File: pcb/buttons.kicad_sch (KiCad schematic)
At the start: 15 parts, among them SW2 PLAY, SW4 STOP, SW5 NEXT, SW6 PREV, SW7 VOLDEC, SW8 VOLINC, SW9 POWER

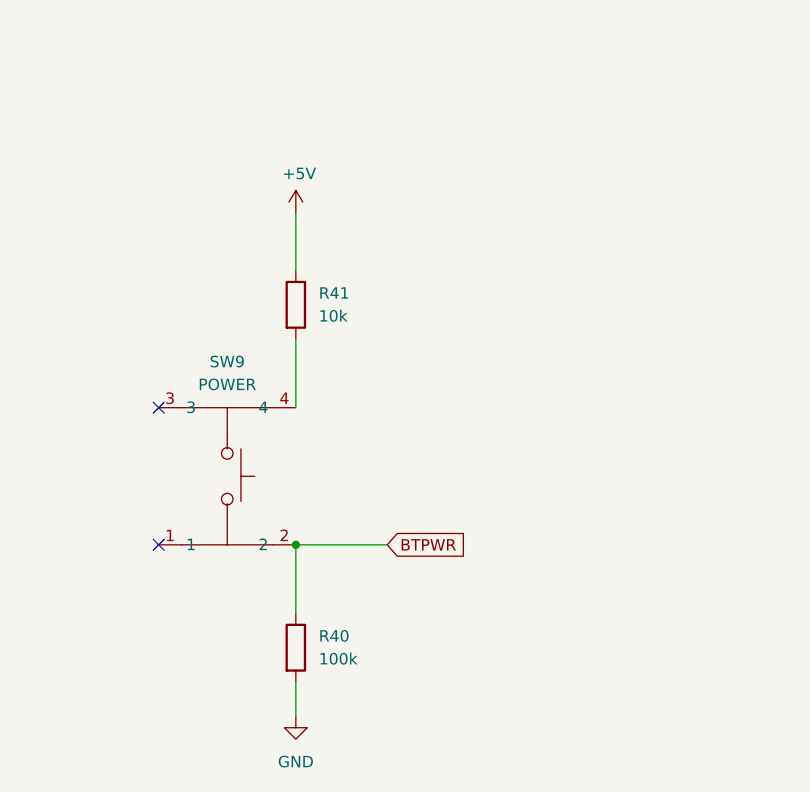
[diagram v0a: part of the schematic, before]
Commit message: Added last minor patches like ideal diode on PCB, added backplate
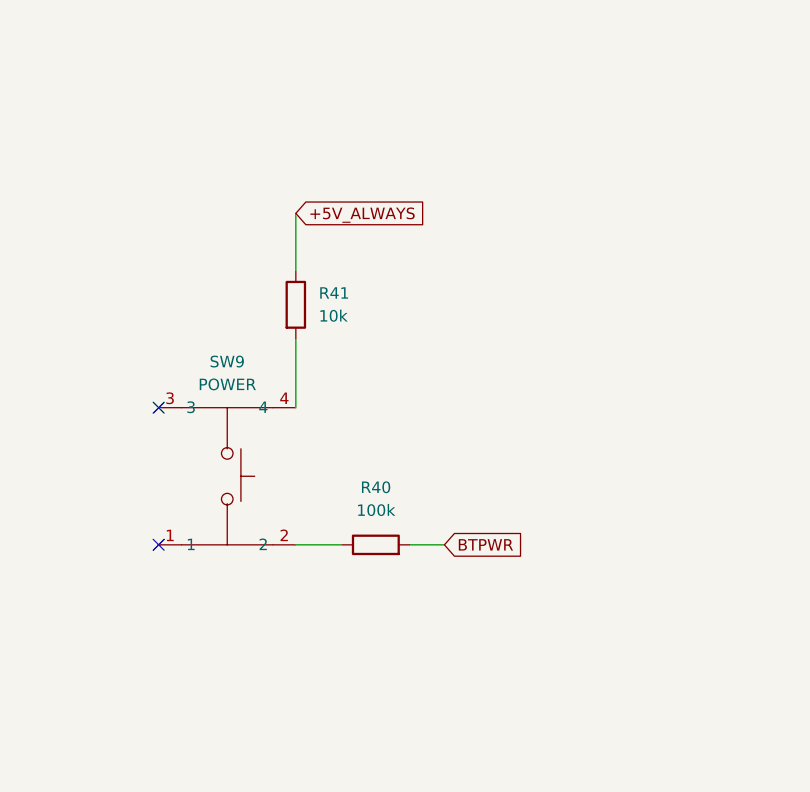
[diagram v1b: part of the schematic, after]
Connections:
- net BTPWR: now also R40.2; no longer R40.1, SW9.2
- net GND: no longer R40.2
- net +5V renamed +5V_ALWAYS
- new net: R40.1, SW9.2
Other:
- moved on the sheet: R40
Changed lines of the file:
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@@
-		(color 0 0 0 0)
-	)
-	(junction
-		(at 78.74 152.4)
-		(diameter 0)
 		(color 0 0 0 0)
 	)
@@
 	(wire
 		(pts
-			(xy 88.9 152.4) (xy 78.74 152.4)
-		)
-		(stroke
-			(width 0)
-			(type default)
-		)
-	)
-	(wire
-		(pts
 			(xy 119.38 49.53) (xy 119.38 57.15)
 		)
@@
 	(wire
 		(pts
-			(xy 78.74 152.4) (xy 78.74 160.02)
+			(xy 91.44 152.4) (xy 95.25 152.4)
 		)
 		(stroke
@@
 	(wire
 		(pts
-			(xy 78.74 167.64) (xy 78.74 171.45)
-		)
-		(stroke
-			(width 0)
-			(type default)
-		)
-	)
-	(wire
-		(pts
 			(xy 156.21 49.53) (xy 168.91 49.53)
 		)
@@
 	(wire
 		(pts
+			(xy 78.74 152.4) (xy 83.82 152.4)
+		)
+		(stroke
+			(width 0)
+			(type default)
+		)
+	)
+	(wire
+		(pts
 			(xy 119.38 49.53) (xy 132.08 49.53)
 		)
@@
 			(width 0)
 			(type default)
+		)
+	)
+	(global_label "+5V_ALWAYS"
+		(shape input)
+		(at 78.74 115.57 0)
+		(fields_autoplaced yes)
+		(effects
+			(font
+				(size 1.27 1.27)
+			)
+			(justify left)
+		)
+		(property "Intersheetrefs" "${INTERSHEET_REFS}"
+			(at 93.5181 115.57 0)
+			(effects
+				(font
+					(size 1.27 1.27)
+				)
+				(justify left)
+				(hide yes)
+			)
 		)
 	)
@@
 	(global_label "BTPWR"
 		(shape input)
-		(at 88.9 152.4 0)
+		(at 95.25 152.4 0)
 		(fields_autoplaced yes)
 		(effects
@@
 		)
 		(property "Intersheetrefs" "${INTERSHEET_REFS}"
-			(at 98.1142 152.4 0)
+			(at 104.4642 152.4 0)
 			(effects
 				(font
@@
 	)
 	(symbol
-		(lib_id "power:+5V")
-		(at 78.74 115.57 0)
-		(unit 1)
-		(exclude_from_sim no)
-		(in_bom yes)
-		(on_board yes)
-		(dnp no)
-		(property "Reference" "#PWR092"
-			(at 78.74 119.38 0)
-			(effects
-				(font
-					(size 1.27 1.27)
-				)
-				(hide yes)
-			)
-		)
-		(property "Value" "+5V"
-			(at 79.121 111.1758 0)
-			(effects
-				(font
-					(size 1.27 1.27)
-				)
-			)
-		)
-		(property "Footprint" ""
-			(at 78.74 115.57 0)
-			(effects
-				(font
-					(size 1.27 1.27)
-				)
-				(hide yes)
-			)
-		)
-		(property "Datasheet" ""
-			(at 78.74 115.57 0)
-			(effects
-				(font
-					(size 1.27 1.27)
-				)
-				(hide yes)
-			)
-		)
-		(property "Description" ""
-			(at 78.74 115.57 0)
-			(effects
-				(font
-					(size 1.27 1.27)
-				)
-				(hide yes)
-			)
-		)
-		(pin "1"
-		)
-		(instances
-			(project "minidisc"
-				(path "/521fcede-69d7-4f6d-a594-609fca379ec3/93b31dc8-efce-45a3-83f8-59a8e0899de6"
-					(reference "#PWR092")
-					(unit 1)
-				)
-			)
-		)
-	)
-	(symbol
 		(lib_id "lcsc:SKSCLAE010")
 		(at 71.12 143.51 0)
@@
 	(symbol
 		(lib_id "Device:R")
-		(at 78.74 163.83 0)
+		(at 87.63 152.4 90)
 		(unit 1)
 		(exclude_from_sim no)
@@
 		(fields_autoplaced yes)
 		(property "Reference" "R40"
-			(at 81.28 162.5599 0)
-			(effects
-				(font
-					(size 1.27 1.27)
-				)
-				(justify left)
+			(at 87.63 146.05 90)
+			(effects
+				(font
+					(size 1.27 1.27)
+				)
 			)
 		)
 		(property "Value" "100k"
-			(at 81.28 165.0999 0)
-			(effects
-				(font
-					(size 1.27 1.27)
-				)
-				(justify left)
+			(at 87.63 148.59 90)
+			(effects
+				(font
+					(size 1.27 1.27)
+				)
 			)
 		)
 		(property "Footprint" "Resistor_SMD:R_0402_1005Metric"
-			(at 76.962 163.83 90)
+			(at 87.63 154.178 90)
 			(effects
 				(font
@@
 		)
 		(property "Datasheet" "~"
-			(at 78.74 163.83 0)
+			(at 87.63 152.4 0)
 			(effects
 				(font
@@
 		)
 		(property "Description" "Resistor"
-			(at 78.74 163.83 0)
+			(at 87.63 152.4 0)
 			(effects
 				(font
@@
 					(unit 1)
 				)
-			)
-		)
-	)
-	(symbol
-		(lib_id "power:GND")
-		(at 78.74 171.45 0)
-		(unit 1)
-		(exclude_from_sim no)
-		(in_bom yes)
-		(on_board yes)
-		(dnp no)
-		(fields_autoplaced yes)
-		(property "Reference" "#PWR091"
-			(at 78.74 177.8 0)
-			(effects
-				(font
-					(size 1.27 1.27)
-				)
-				(hide yes)
-			)
-		)
-		(property "Value" "GND"
-			(at 78.74 176.53 0)
-			(effects
-				(font
-					(size 1.27 1.27)
-				)
-			)
-		)
-		(property "Footprint" ""
-			(at 78.74 171.45 0)
-			(effects
-				(font
-					(size 1.27 1.27)
-				)
-				(hide yes)
-			)
-		)
-		(property "Datasheet" ""
-			(at 78.74 171.45 0)
-			(effects
-				(font
-					(size 1.27 1.27)
-				)
-				(hide yes)
-			)
-		)
-		(property "Description" ""
-			(at 78.74 171.45 0)
-			(effects
-				(font
-					(size 1.27 1.27)
-				)
-				(hide yes)
-			)
-		)
-		(pin "1"
-		)
-		(instances
-			(project "minidisc"
-				(path "/521fcede-69d7-4f6d-a594-609fca379ec3/93b31dc8-efce-45a3-83f8-59a8e0899de6"
-					(reference "#PWR091")
-					(unit 1)
-				)
